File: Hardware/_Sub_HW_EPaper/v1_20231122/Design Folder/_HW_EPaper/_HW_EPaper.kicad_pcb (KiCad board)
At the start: 2 copper layers, 0 parts

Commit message: Latest update
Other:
- board outline added: 49.5 x 49.5 mm
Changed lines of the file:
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@@
   )
   (net 0 "")
+  (gr_rect (start 101.6 114.3) (end 151.13 163.83)
+    (stroke (width 0.1) (type default)) (fill none) (layer "Edge.Cuts"))
 )

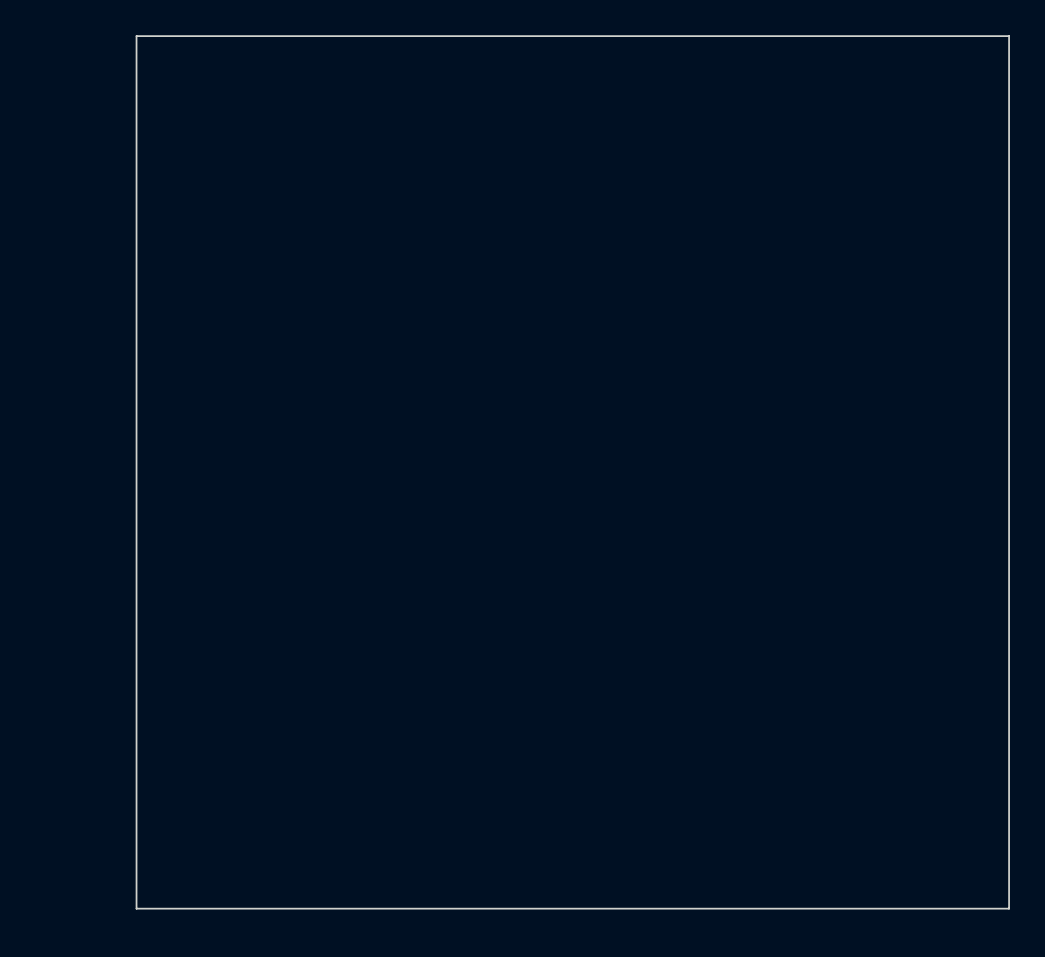
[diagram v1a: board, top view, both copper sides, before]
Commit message: Working on epaper hardware
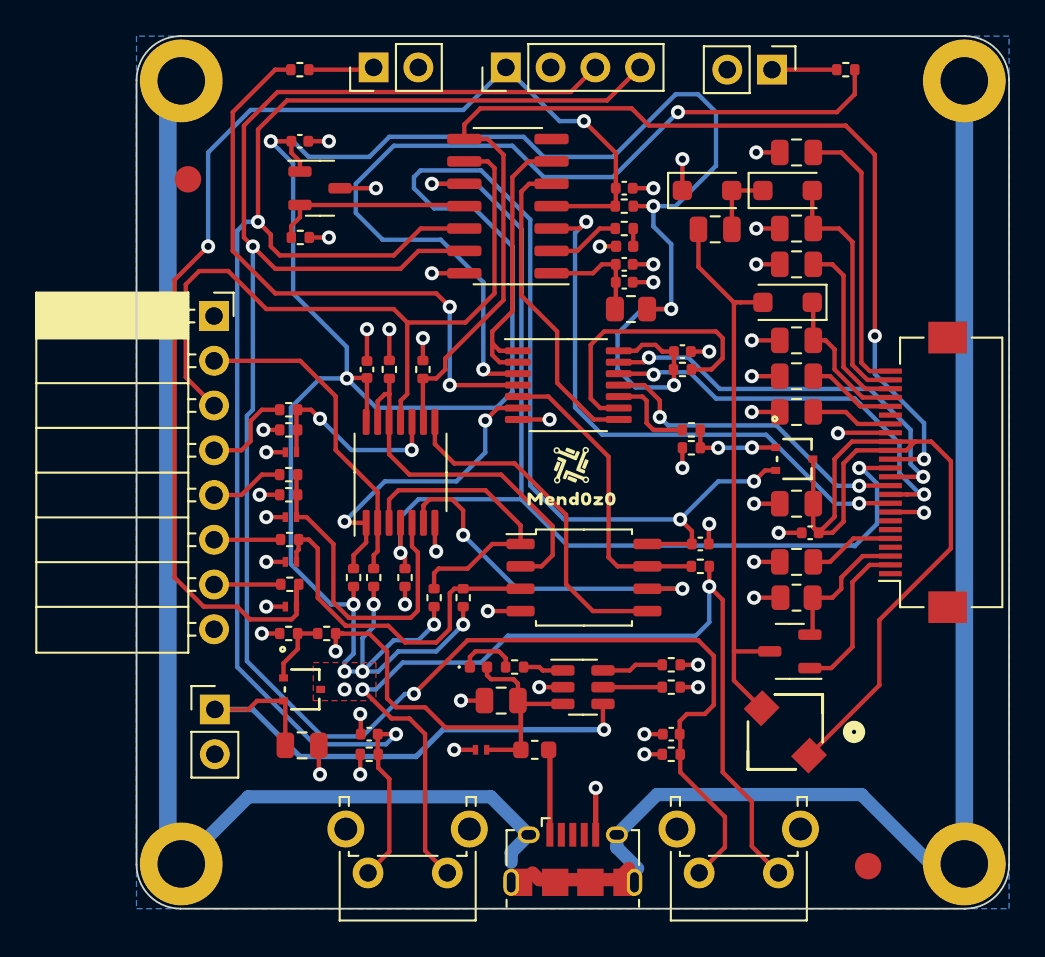
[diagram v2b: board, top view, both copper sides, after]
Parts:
- added C1001: 4u7F_16V, Capacitor_SMD:C_0805_2012Metric, F.Cu at (111.0, 154.6)
- added C1002: 4u7F_16V, Capacitor_SMD:C_0805_2012Metric, F.Cu at (122.3, 152.0)
- added C301: 100nF_50V, Capacitor_SMD:C_0402_1005Metric, F.Cu at (129.3, 122.9)
- added C302: 1uF_10V_X7R, Capacitor_SMD:C_0402_1005Metric, F.Cu at (129.3, 127.3)
- added C303: 100nF_50V, Capacitor_SMD:C_0402_1005Metric, F.Cu at (129.3, 128.3)
- added C401: 1uF_10V_X7R, Capacitor_SMD:C_0402_1005Metric, F.Cu at (133.6, 143.1)
- added C501: 1uF_10V_X7R, Capacitor_SMD:C_0402_1005Metric, F.Cu at (114.7, 133.2)
- added C601: 1uF_10V_X7R, Capacitor_SMD:C_0402_1005Metric, F.Cu at (132.6, 132.2)
- added C701: 4u7F_16V, Capacitor_SMD:C_0805_2012Metric, F.Cu at (139.1, 144.1)
- added C702: 4u7F_16V, Capacitor_SMD:C_0805_2012Metric, F.Cu at (139.1, 140.8)
- added C703: 100nF_50V, Capacitor_SMD:C_0402_1005Metric, F.Cu at (139.8, 142.5)
- added C704: 4u7F_16V, Capacitor_SMD:C_0805_2012Metric, F.Cu at (139.1, 135.6)
- added C705: 4u7F_16V, Capacitor_SMD:C_0805_2012Metric, F.Cu at (139.1, 131.6)
- added C706: 4u7F_16V, Capacitor_SMD:C_0805_2012Metric, F.Cu at (139.1, 133.6)
- added C707: 4u7F_16V, Capacitor_SMD:C_0805_2012Metric, F.Cu at (139.1, 127.3)
- added C708: 4u7F_16V, Capacitor_SMD:C_0805_2012Metric, F.Cu at (134.4, 125.3)
- added C709: 4u7F_16V, Capacitor_SMD:C_0805_2012Metric, F.Cu at (139.1, 120.9)
- added C710: 4u7F_16V, Capacitor_SMD:C_0805_2012Metric, F.Cu at (139.1, 125.2)
- added C801: 1uF_10V_X7R, Capacitor_SMD:C_0402_1005Metric, F.Cu at (132.0, 153.9)
- added C802: 1uF_10V_X7R, Capacitor_SMD:C_0402_1005Metric, F.Cu at (114.8, 153.9)
- added C901: 1uF_10V_X7R, Capacitor_SMD:C_0402_1005Metric, F.Cu at (110.9, 120.3)
- added D1001: TVS_6.5V_3A, _PCBLIB_Epaper:CR_7PCT_L3F_TOS, F.Cu at (121.2, 154.8)
- added D501: TVS_6.5V_3A, _PCBLIB_Epaper:CR_7PCT_L3F_TOS, F.Cu at (110.4, 141.6)
- added D502: TVS_6.5V_3A, _PCBLIB_Epaper:CR_7PCT_L3F_TOS, F.Cu at (110.4, 137.9)
- added D503: TVS_6.5V_3A, _PCBLIB_Epaper:CR_7PCT_L3F_TOS, F.Cu at (110.4, 144.1)
- added D504: TVS_6.5V_3A, _PCBLIB_Epaper:CR_7PCT_L3F_TOS, F.Cu at (110.4, 146.7)
- added D701: SS2040FL, Diode_SMD:D_SOD-123F, F.Cu at (138.6, 129.4)
- added D702: SS2040FL, Diode_SMD:D_SOD-123F, F.Cu at (138.6, 123.1)
- added D703: SS2040FL, Diode_SMD:D_SOD-123F, F.Cu at (134.0, 123.1)
- added F1001: 100mA_15V_0.5R, Fuse:Fuse_0603_1608Metric, F.Cu at (124.2, 154.8)
- added FD1201: 1.5mmX3mm, Fiducial:Fiducial_1.5mm_Mask3mm, F.Cu at (104.5, 122.4)
- added FD1202: 1.5mmX3mm, Fiducial:Fiducial_1.5mm_Mask3mm, F.Cu at (143.1, 161.4)
- added GR1201: Mend0z0 Logo, _PCBLIB_Epaper:LOGO_MEND0Z0, F.Cu at (126.4, 139.1)
- added J1001: USB_microB_RA, Connector_USB:USB_Micro-B_Amphenol_10118194_Horizontal, F.Cu at (126.4, 161.0)
- added J1002: HDR_2POS_VERT, Connector_PinHeader_2.54mm:PinHeader_1x02_P2.54mm_Vertical, F.Cu at (106.0, 152.5)
- added J1101: HDR_2POS_VERT, Connector_PinHeader_2.54mm:PinHeader_1x02_P2.54mm_Vertical, F.Cu at (115.1, 116.1)
- added J1102: HDR_2POS_VERT, Connector_PinHeader_2.54mm:PinHeader_1x02_P2.54mm_Vertical, F.Cu at (137.7, 116.2)
- added J301: HDR_4POS_VERT, Connector_PinHeader_2.54mm:PinHeader_1x04_P2.54mm_Vertical, F.Cu at (122.6, 116.1)
- added J501: RECEPT_8POS_RA, Connector_PinSocket_2.54mm:PinSocket_1x08_P2.54mm_Horizontal, F.Cu at (106.0, 130.2)
- added J701: FPC_24POS_BOTTOM_0.5P, Connector_FFC-FPC:Hirose_FH12-24S-0.5SH_1x24-1MP_P0.50mm_Horizontal, F.Cu at (146.2, 139.1)
- added L701: 10uH_600mA, _PCBLIB_Epaper:IND_CDRH3D11HPNP-100NC_SUM, F.Cu at (138.4, 153.8)
- added LED1001: RED_2V, LED_SMD:LED_0402_1005Metric, F.Cu at (121.0, 150.1)
- added LED301: RED_2V, LED_SMD:LED_0402_1005Metric, F.Cu at (129.3, 126.2)
- added MH1201: M2.5_DIN965, MountingHole:MountingHole_2.7mm_M2.5_DIN965_Pad, F.Cu at (148.6, 161.3)
- added MH1202: M2.5_DIN965, MountingHole:MountingHole_2.7mm_M2.5_DIN965_Pad, F.Cu at (148.6, 116.8)
- added MH1203: M2.5_DIN965, MountingHole:MountingHole_2.7mm_M2.5_DIN965_Pad, F.Cu at (104.1, 161.3)
- added MH1204: M2.5_DIN965, MountingHole:MountingHole_2.7mm_M2.5_DIN965_Pad, F.Cu at (104.1, 116.8)
- added Q1001: SSM3J117TU,LF, _PCBLIB_Epaper:UFM_TOS, F.Cu at (111.0, 151.4)
- added Q701: AS3400, Package_TO_SOT_SMD:SOT-23-3, F.Cu at (138.7, 149.2)
- added Q702: SSM3J117TU,LF, _PCBLIB_Epaper:UFM_TOS, F.Cu at (138.9, 138.3)
- added R1001: 100R_1/10W_1%, Resistor_SMD:R_0402_1005Metric, F.Cu at (123.1, 150.1)
- added R1002: 30kR_1/16W_1%, Resistor_SMD:R_0402_1005Metric, F.Cu at (132.0, 151.3)
- added R1003: 10kR_1/16W_1%, Resistor_SMD:R_0402_1005Metric, F.Cu at (132.0, 150.0)
- added R1004: 470R_1/16W_1%, Resistor_SMD:R_0402_1005Metric, F.Cu at (112.4, 148.2)
- added R1005: 10kR_1/16W_1%, Resistor_SMD:R_0402_1005Metric, F.Cu at (110.2, 148.2)
- added R1101: 100R_1/10W_1%, Resistor_SMD:R_0402_1005Metric, F.Cu at (110.9, 116.2)
- added R1102: 100R_1/10W_1%, Resistor_SMD:R_0402_1005Metric, F.Cu at (141.9, 116.2)
- added R301: 10kR_1/16W_1%, Resistor_SMD:R_0402_1005Metric, F.Cu at (129.3, 124.0)
- added R302: 470R_1/16W_1%, Resistor_SMD:R_0402_1005Metric, F.Cu at (129.3, 125.2)
- added R303: 1R_1/4W_1%, Resistor_SMD:R_0805_2012Metric, F.Cu at (129.7, 129.8)
- added R401: 10kR_1/16W_1%, Resistor_SMD:R_0402_1005Metric, F.Cu at (118.5, 146.2)
- added R402: 10kR_1/16W_1%, Resistor_SMD:R_0402_1005Metric, F.Cu at (120.1, 146.2)
- added R403: 10kR_1/16W_1%, Resistor_SMD:R_0402_1005Metric, F.Cu at (133.6, 144.4)
- added R501: 10kR_1/16W_1%, Resistor_SMD:R_0402_1005Metric, F.Cu at (115.1, 145.0)
- added R502: 10kR_1/16W_1%, Resistor_SMD:R_0402_1005Metric, F.Cu at (113.9, 145.0)
- added R503: 27R_1/16W_1%, Resistor_SMD:R_0402_1005Metric, F.Cu at (110.2, 139.2)
- added R504: 27R_1/16W_1%, Resistor_SMD:R_0402_1005Metric, F.Cu at (110.2, 135.5)
- added R505: 10kR_1/16W_1%, Resistor_SMD:R_0402_1005Metric, F.Cu at (110.2, 140.3)
- added R506: 10kR_1/16W_1%, Resistor_SMD:R_0402_1005Metric, F.Cu at (116.8, 145.0)
- added R507: 10kR_1/16W_1%, Resistor_SMD:R_0402_1005Metric, F.Cu at (116.0, 133.2)
- added R508: 10kR_1/16W_1%, Resistor_SMD:R_0402_1005Metric, F.Cu at (110.2, 136.7)
- added R509: 10kR_1/16W_1%, Resistor_SMD:R_0402_1005Metric, F.Cu at (117.9, 133.2)
- added R510: 27R_1/16W_1%, Resistor_SMD:R_0402_1005Metric, F.Cu at (110.3, 142.9)
- added R511: 27R_1/16W_1%, Resistor_SMD:R_0402_1005Metric, F.Cu at (110.3, 145.4)
- added R601: 10kR_1/16W_1%, Resistor_SMD:R_0402_1005Metric, F.Cu at (132.6, 133.2)
- added R701: 0.47R_1/8W_5%, Resistor_SMD:R_0805_2012Metric, F.Cu at (139.1, 146.2)
- added R702: 470R_1/16W_1%, Resistor_SMD:R_0402_1005Metric, F.Cu at (133.1, 136.7)
- added R703: 10kR_1/16W_1%, Resistor_SMD:R_0402_1005Metric, F.Cu at (133.1, 137.7)
- added R801: 10kR_1/16W_1%, Resistor_SMD:R_0402_1005Metric, F.Cu at (132.0, 155.1)
- added R802: 10kR_1/16W_1%, Resistor_SMD:R_0402_1005Metric, F.Cu at (114.8, 155.1)
- added R901: 10kR_1/16W_1%, Resistor_SMD:R_0402_1005Metric, F.Cu at (110.9, 125.7)
- added SW801: SPST-NO, Button_Switch_THT:SW_Tactile_SPST_Angled_PTS645Vx31-2LFS, F.Cu at (138.0, 161.8)
- added SW802: SPST-NO, Button_Switch_THT:SW_Tactile_SPST_Angled_PTS645Vx31-2LFS, F.Cu at (119.2, 161.8)
- added U1001: RT9526AGE, Package_TO_SOT_SMD:SOT-23-6, F.Cu at (126.9, 151.3)
- added U301: PIC16F15223_8BIT, Package_SO:SO-14_3.9x8.65mm_P1.27mm, F.Cu at (122.7, 124.0)
- added U401: W25Q64JVSSIQ, Package_SO:SOIC-8_5.23x5.23mm_P1.27mm, F.Cu at (127.0, 145.0)
- added U501: SN74HCS32PWR, Package_SO:TSSOP-14_4.4x5mm_P0.65mm, F.Cu at (116.6, 139.1)
- added U601: 74VHC164FT, Package_SO:TSSOP-14_4.4x5mm_P0.65mm, F.Cu at (126.1, 134.1)
- added U901: MCP9700T-E/TT, Package_TO_SOT_SMD:SOT-23-3, F.Cu at (112.0, 122.9)
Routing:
- net /BLOCK DIAGRAM/BATTERY CIRCUIT/V_BATT: track 0.00 -> 248.6 mm, vias 0 -> 16
- net Earth: track 0.00 -> 144.7 mm
- net /BLOCK DIAGRAM/MCU/PIC_ICSPDAT: track 0.00 -> 111.3 mm, vias 0 -> 2
- net /BLOCK DIAGRAM/MCU/PIC_ICSPCLK: track 0.00 -> 88.8 mm, vias 0 -> 2
- net /BLOCK DIAGRAM/MCU/PIC_~{MCLR}: track 0.00 -> 69.7 mm, vias 0 -> 2
- net GND: track 0.00 -> 68.4 mm, vias 0 -> 49
- net /BLOCK DIAGRAM/DISPLAY DRIVER/SPI_SDO: track 0.00 -> 66.1 mm, vias 0 -> 2
- net /BLOCK DIAGRAM/DISPLAY DRIVER/SPI_CLK: track 0.00 -> 62.6 mm, vias 0 -> 3
- net /BLOCK DIAGRAM/LED DRIVER/LED_2: track 0.00 -> 50.8 mm, vias 0 -> 2
- net Net-(C702-Pad1): track 0.00 -> 46.0 mm
- net /BLOCK DIAGRAM/INPUT CIRCUIT/EXTERNAL_SPI_MISO: track 0.00 -> 42.1 mm
- net /BLOCK DIAGRAM/LED DRIVER/LED_1: track 0.00 -> 34.1 mm, vias 0 -> 2
- net /BLOCK DIAGRAM/DISPLAY DRIVER/E24_BUSY: track 0.00 -> 33.1 mm, vias 0 -> 2
- net Net-(C708-Pad1): track 0.00 -> 32.4 mm
- net /BLOCK DIAGRAM/BATTERY CIRCUIT/RT_BATT: track 0.00 -> 32.0 mm, vias 0 -> 1
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- added copper zone on F.Cu, net /BLOCK DIAGRAM/BATTERY CIRCUIT/V_BATT
- added copper zone on B.Cu, net GND
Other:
- outline, holes or cut-outs redrawn

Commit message: Hardware is almost done
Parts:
- J1001: footprint Connector_USB:USB_Micro-B_Amphenol_10118194_Horizontal -> _PCBLIB_Epaper:USB_Micro-B_Amphenol_10118194_Horizontal
- J501: value RECEPT_8POS_RA -> HDR_8POS_RA; footprint Connector_PinSocket_2.54mm:PinSocket_1x08_P2.54mm_Horizontal -> Connector_PinHeader_2.54mm:PinHeader_1x08_P2.54mm_Horizontal
- Q701, U901: footprint Package_TO_SOT_SMD:SOT-23-3 -> Package_TO_SOT_SMD:SOT-23
- U401: footprint Package_SO:SOIC-8_5.23x5.23mm_P1.27mm -> Package_SO:SOIC-8_5.275x5.275mm_P1.27mm
- moved J501 17.8 mm to (106.0, 148.0), turned to 180 degrees
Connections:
- J501 pad 2: /BLOCK DIAGRAM/INPUT CIRCUIT/EXTERNAL_SPI_~{CS} -> /BLOCK DIAGRAM/INPUT CIRCUIT/EXTERNAL_MCU_~{MCLR}
- J501 pad 3: /BLOCK DIAGRAM/INPUT CIRCUIT/EXTERNAL_SPI_MISO -> /BLOCK DIAGRAM/INPUT CIRCUIT/EXTERNAL_EEPROM_~{WP}
- J501 pad 4: /BLOCK DIAGRAM/INPUT CIRCUIT/EXTERNAL_SPI_MOSI -> /BLOCK DIAGRAM/INPUT CIRCUIT/EXTERNAL_SPI_SCK
- J501 pad 5: /BLOCK DIAGRAM/INPUT CIRCUIT/EXTERNAL_SPI_SCK -> /BLOCK DIAGRAM/INPUT CIRCUIT/EXTERNAL_SPI_MOSI
- J501 pad 6: /BLOCK DIAGRAM/INPUT CIRCUIT/EXTERNAL_EEPROM_~{WP} -> /BLOCK DIAGRAM/INPUT CIRCUIT/EXTERNAL_SPI_MISO
- J501 pad 7: /BLOCK DIAGRAM/INPUT CIRCUIT/EXTERNAL_MCU_~{MCLR} -> /BLOCK DIAGRAM/INPUT CIRCUIT/EXTERNAL_SPI_~{CS}
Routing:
- net /BLOCK DIAGRAM/BATTERY CIRCUIT/V_BATT: track 248.6 -> 252.2 mm
- net /BLOCK DIAGRAM/BATTERY CIRCUIT/VBUS: track 27.5 -> 25.2 mm, vias 1 -> 0
- net /BLOCK DIAGRAM/INPUT CIRCUIT/SF_DO: track 21.0 -> 21.9 mm
- net /BLOCK DIAGRAM/INPUT CIRCUIT/SF_~{CS}: track 17.4 -> 17.9 mm
- net Earth: track 144.7 -> 144.1 mm
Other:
- board text added: "+ -"
- board text added: "- + LED2"
- board text added: "BATT +3V7"
- board text added: "BATT CHRG IND"
- board text added: "BOTT"
- board text added: "Display < 5{dblquote}"
- board text added: "GND ~{MCLR} ~{WP} SCK MOSI MISO ~{CS} GND"
- board text added: "LED1 + -"
- board text added: "M2.5"
- board text added: "MCU PRCS IND"
- board text added: "PCB Layout"
- board text added: "PRELIMINARY"
- board text added: "Prj: _HW_EPaper Ver: v1.0 Date: 23/12/18 DES: SiavashTP"
- board text added: "UP"
- board text added: "~{MCLR} GND DAT CLK"

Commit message: Updating file templates and structures...
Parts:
- moved C1001 88.6 mm to (149.2, 234.5)
- moved C1002 88.6 mm to (160.5, 231.9)
- moved C601 88.6 mm to (170.8, 212.1)
- moved C702 88.6 mm to (177.2, 220.8)
- moved C703 88.6 mm to (178.0, 222.4)
- moved C704 88.6 mm to (177.2, 215.6)
- moved C705 88.6 mm to (177.2, 211.5)
- moved C708 88.6 mm to (172.6, 205.2)
- moved C709 88.6 mm to (177.2, 200.8)
- moved C801 88.6 mm to (170.1, 233.8)
- moved C802 88.6 mm to (153.0, 233.8)
- moved C901 88.6 mm to (149.0, 200.2)
- moved D1001 88.6 mm to (159.3, 234.7)
- moved D501 88.6 mm to (148.5, 221.5)
- moved D502 88.6 mm to (148.5, 217.8)
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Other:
- board text removed: "PCB Layout"
- board text removed: "PRELIMINARY"

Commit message: Updating Hardware File structures
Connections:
- net /BLOCK DIAGRAM/BATTERY CIRCUIT/RT_BATT renamed /BLOCK DIAGRAM/BATTERY CHARGER/RT_BATT
- net /BLOCK DIAGRAM/BATTERY CIRCUIT/RT_CHG_SB renamed /BLOCK DIAGRAM/BATTERY CHARGER/RT_CHG_SB
- net /BLOCK DIAGRAM/BATTERY CIRCUIT/RT_IMIN renamed /BLOCK DIAGRAM/BATTERY CHARGER/RT_IMIN
- net /BLOCK DIAGRAM/BATTERY CIRCUIT/RT_ISET renamed /BLOCK DIAGRAM/BATTERY CHARGER/RT_ISET
- net /BLOCK DIAGRAM/BATTERY CIRCUIT/VBUS renamed /BLOCK DIAGRAM/BATTERY CHARGER/VBUS
- net /BLOCK DIAGRAM/BATTERY CIRCUIT/V_BATT renamed /BLOCK DIAGRAM/BATTERY CHARGER/V_BATT
- net /BLOCK DIAGRAM/MCU/IND_LED renamed /BLOCK DIAGRAM/MICROCONTROLLER/IND_LED
- net /BLOCK DIAGRAM/MCU/PIC_ICSPCLK renamed /BLOCK DIAGRAM/MICROCONTROLLER/PIC_ICSPCLK
- net /BLOCK DIAGRAM/MCU/PIC_ICSPDAT renamed /BLOCK DIAGRAM/MICROCONTROLLER/PIC_ICSPDAT
- net /BLOCK DIAGRAM/MCU/PIC_~{MCLR} renamed /BLOCK DIAGRAM/MICROCONTROLLER/PIC_~{MCLR}
- net /BLOCK DIAGRAM/MCU/SIPO_CLK renamed /BLOCK DIAGRAM/MICROCONTROLLER/SIPO_CLK
- net /BLOCK DIAGRAM/MCU/SIPO_DATA renamed /BLOCK DIAGRAM/MICROCONTROLLER/SIPO_DATA
- net /BLOCK DIAGRAM/MCU/TEMP_ADC renamed /BLOCK DIAGRAM/MICROCONTROLLER/TEMP_ADC
- net /BLOCK DIAGRAM/SIPO/74VHC164_~{CLR} renamed /BLOCK DIAGRAM/SHIFT REGISTER (SIPO)/74VHC164_~{CLR}
